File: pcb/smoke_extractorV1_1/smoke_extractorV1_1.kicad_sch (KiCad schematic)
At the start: 7 parts

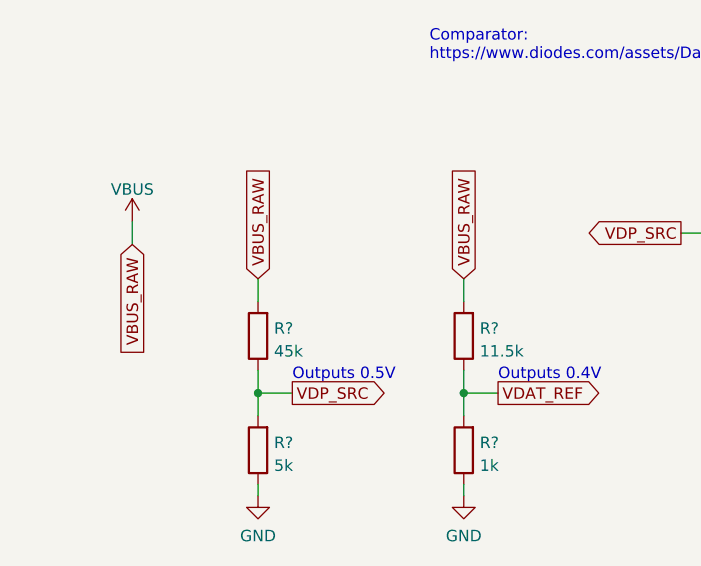
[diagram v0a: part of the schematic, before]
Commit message: Added the first comparator for the USB Data lines
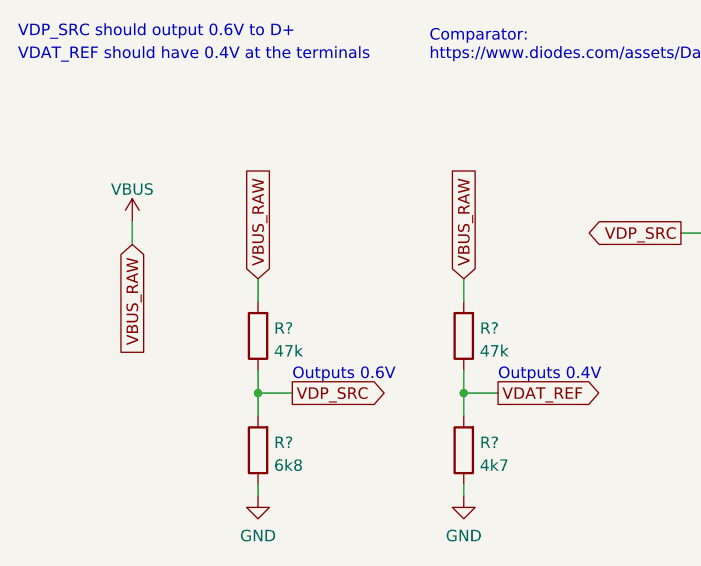
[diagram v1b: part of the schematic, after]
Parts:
- R?: value 1k -> 4k7
- R?: value 11.5k -> 47k
- R?: value 45k -> 47k
- R?: value 5k -> 6k8
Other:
- note added: "Outputs 0.6V"
- note added: "VDAT_REF should have 0.4V at the terminals"
- note added: "VDP_SRC should output 0.6V to D+"
- note removed: "Outputs 0.5V"
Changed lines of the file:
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@@
     (stroke (width 0) (type default) (color 0 0 0 0))
   )
+  (text "VDAT_REF should have 0.4V at the terminals\n" (at 12.7 6.35 0)
+    (effects (font (size 1.27 1.27)) (justify left bottom))
+  )
   (text "Outputs 0.4V" (at 66.04 41.91 0)
     (effects (font (size 1.27 1.27)) (justify left bottom))
   )
-  (text "Outputs 0.5V" (at 43.18 41.91 0)
+  (text "VDP_SRC should output 0.6V to D+" (at 12.7 3.81 0)
+    (effects (font (size 1.27 1.27)) (justify left bottom))
+  )
+  (text "Outputs 0.6V" (at 43.18 41.91 0)
     (effects (font (size 1.27 1.27)) (justify left bottom))
   )
@@
       (effects (font (size 1.27 1.27)) (justify right))
     )
-    (property "Value" "1k" (id 1) (at 64.008 51.2322 0)
+    (property "Value" "4k7" (id 1) (at 64.008 51.2322 0)
       (effects (font (size 1.27 1.27)) (justify right))
     )
@@
       (effects (font (size 1.27 1.27)) (justify right))
     )
-    (property "Value" "11.5k" (id 1) (at 64.008 38.5322 0)
+    (property "Value" "47k" (id 1) (at 64.008 38.5322 0)
       (effects (font (size 1.27 1.27)) (justify right))
     )
@@
       (effects (font (size 1.27 1.27)) (justify right))
     )
-    (property "Value" "45k" (id 1) (at 41.148 38.5322 0)
+    (property "Value" "47k" (id 1) (at 41.148 38.5322 0)
       (effects (font (size 1.27 1.27)) (justify right))
     )
@@
       (effects (font (size 1.27 1.27)) (justify right))
     )
-    (property "Value" "5k" (id 1) (at 41.148 51.2322 0)
+    (property "Value" "6k8" (id 1) (at 41.148 51.2322 0)
       (effects (font (size 1.27 1.27)) (justify right))
     )
@@
     )
     (path "/003a3556-27e1-4c94-8336-eff7b2d2f9bb"
-      (reference "R?") (unit 1) (value "1k") (footprint "")
+      (reference "R?") (unit 1) (value "4k7") (footprint "")
     )
     (path "/380a39d0-b84f-4b62-87a9-847ecd2b9168"
-      (reference "R?") (unit 1) (value "11.5k") (footprint "")
+      (reference "R?") (unit 1) (value "47k") (footprint "")
     )
     (path "/56ce3fcd-62bc-4dba-a6b1-ae8205ebf6db"
-      (reference "R?") (unit 1) (value "45k") (footprint "")
+      (reference "R?") (unit 1) (value "47k") (footprint "")
     )
     (path "/b683cc23-b225-4f7c-ab01-f58eb518a6d4"
@@
     )
     (path "/e38d534d-2172-4396-955c-5f0a970e41ae"
-      (reference "R?") (unit 1) (value "5k") (footprint "")
+      (reference "R?") (unit 1) (value "6k8") (footprint "")
     )
     (path "/e88e7d59-0051-411d-8d9c-5506936fb14d"

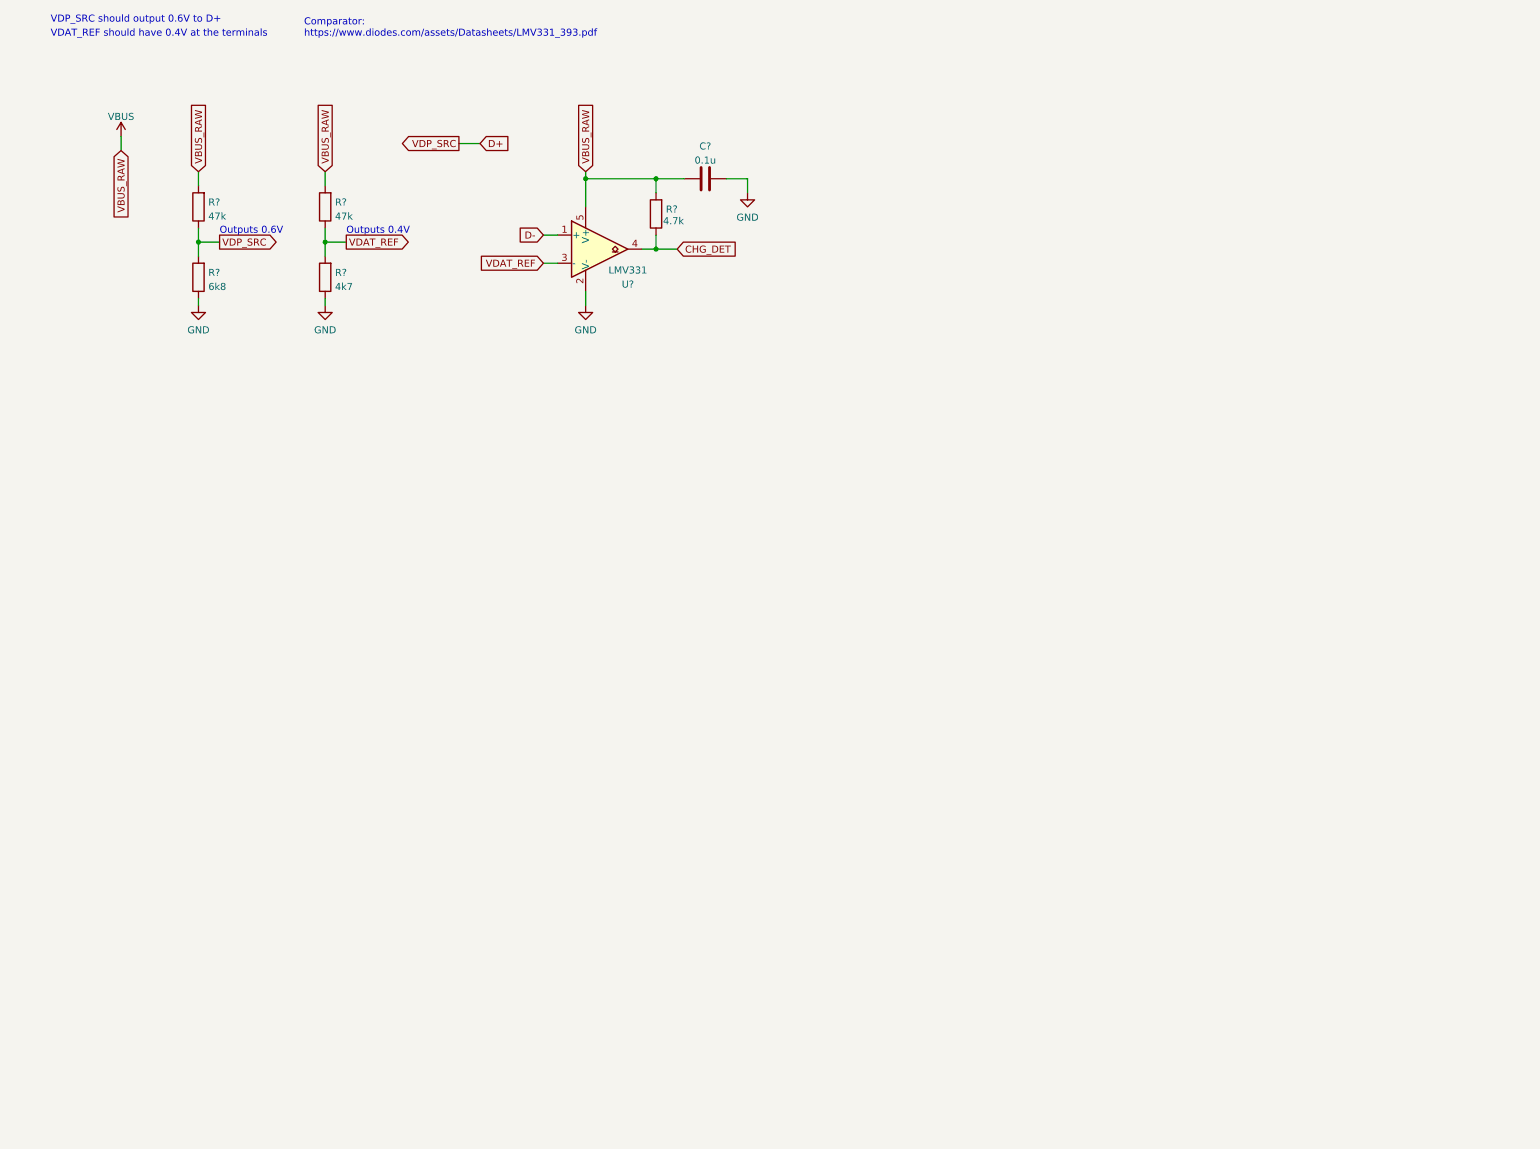
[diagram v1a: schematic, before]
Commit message: Added comparators circuit (D lines and CC lines) to the schematic
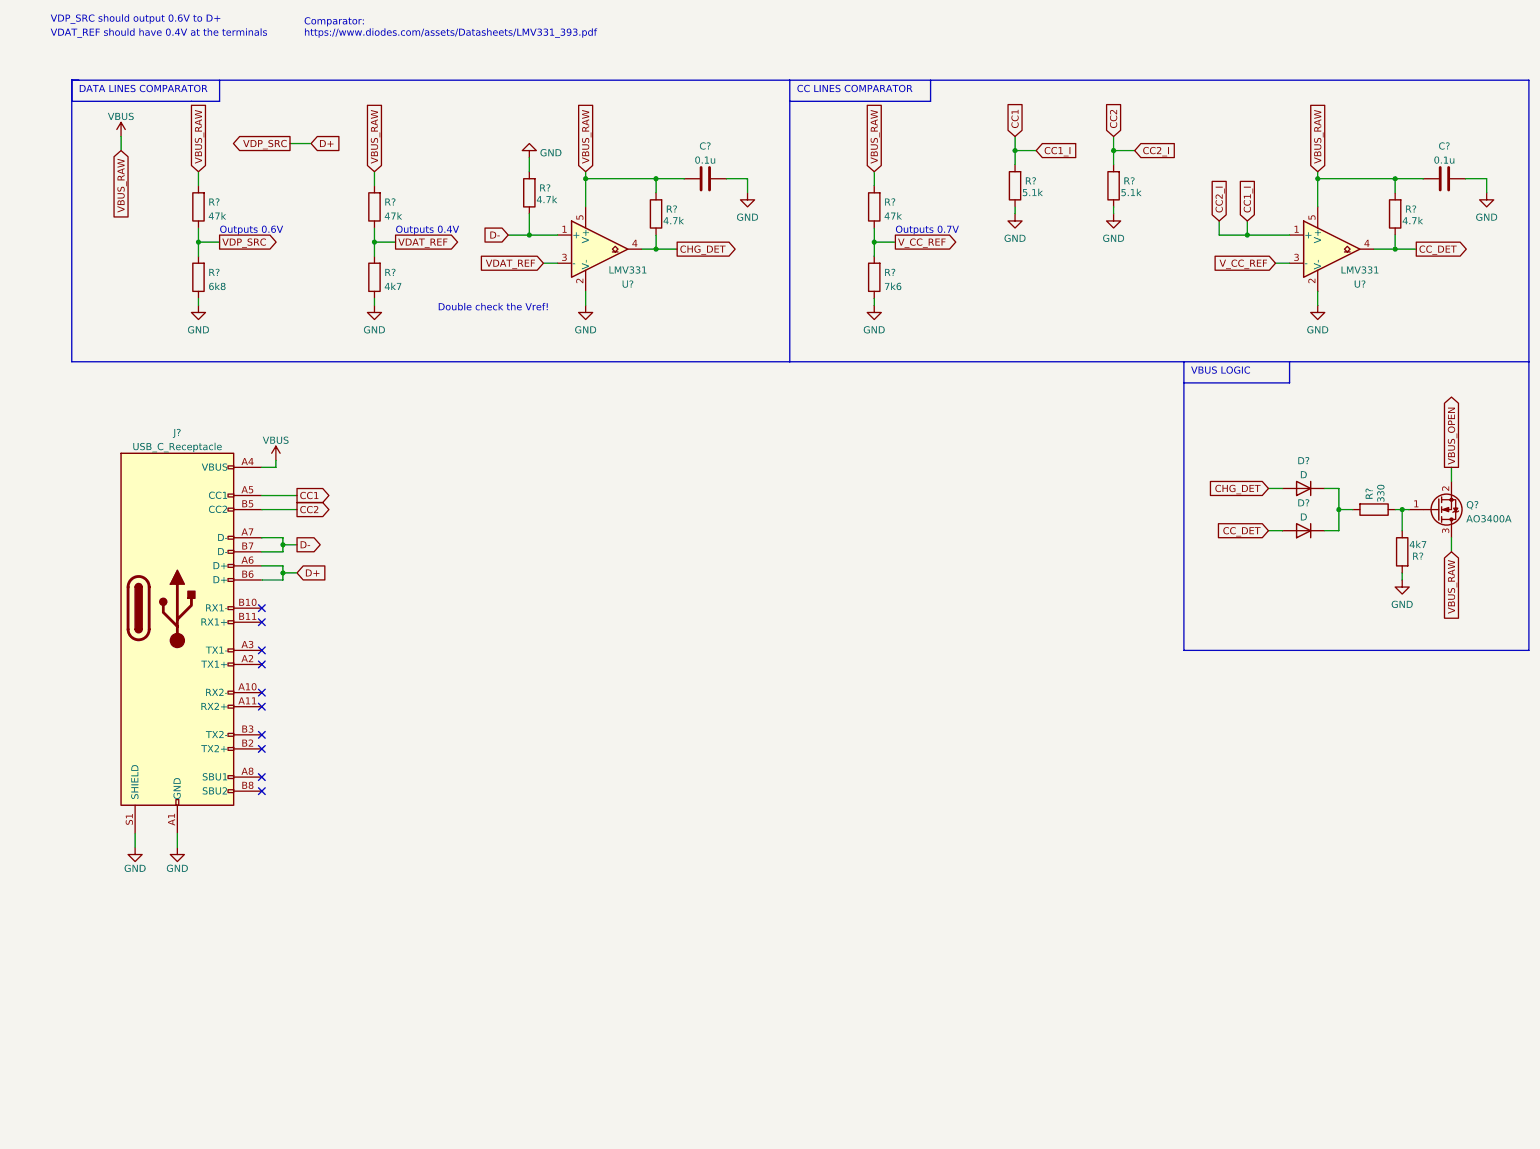
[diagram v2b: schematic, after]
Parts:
- added C?: 0.1u, symbol Device:C
- added D? (x2): D, symbol Device:D
- added J?: USB_C_Receptacle, symbol Connector:USB_C_Receptacle
- added Q?: AO3400A, Package_TO_SOT_SMD:SOT-23, symbol Transistor_FET:AO3400A
- added R?: 4k7, symbol Device:R
- added R? (x2): 5.1k, symbol Device:R
- added R?: 47k, symbol Device:R
- added R? (x2): 4.7k, symbol Device:R
- added R?: 330, symbol Device:R
- added R?: 7k6, symbol Device:R
- added U?: LMV331, symbol Comparator:LMV331
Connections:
- net CHG_DET: now also D?.2 (A)
- net D+: now also J?.A6 (D+), J?.B6 (D+)
- net D-: now also J?.A7 (D-), J?.B7 (D-), R?.1
- net GND: now also C?.2, J?.A1 (GND), J?.A12 (GND), J?.B1 (GND), J?.B12 (GND), J?.S1 (SHIELD), R?.1, R?.1, R?.1, R?.2, R?.2, U?.2 (V-)
- net VBUS: now also C?.1, J?.A4 (VBUS), J?.A9 (VBUS), J?.B4 (VBUS), J?.B9 (VBUS), Q?.3 (D), R?.2, R?.2, U?.5 (V+)
- new net: Q?.1 (G), R?.1, R?.1
- new net: D?.1 (K), D?.1 (K), R?.2
- new net CC1: J?.A5 (CC1), J?.B5 (CC2), R?.2, R?.2, U?.1 (+)
- new net CC_DET: D?.2 (A), R?.1, U?.4
- new net VBUS_OPEN: Q?.2 (S)
- new net V_CC_REF: R?.1, R?.2, U?.3 (-)
- no-connect marks 0 -> 10
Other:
- note added: "CC LINES COMPARATOR"
- note added: "DATA LINES COMPARATOR"
- note added: "Double check the Vref!"
- note added: "Outputs 0.7V"
- note added: "VBUS LOGIC"
- moved on the sheet: R?

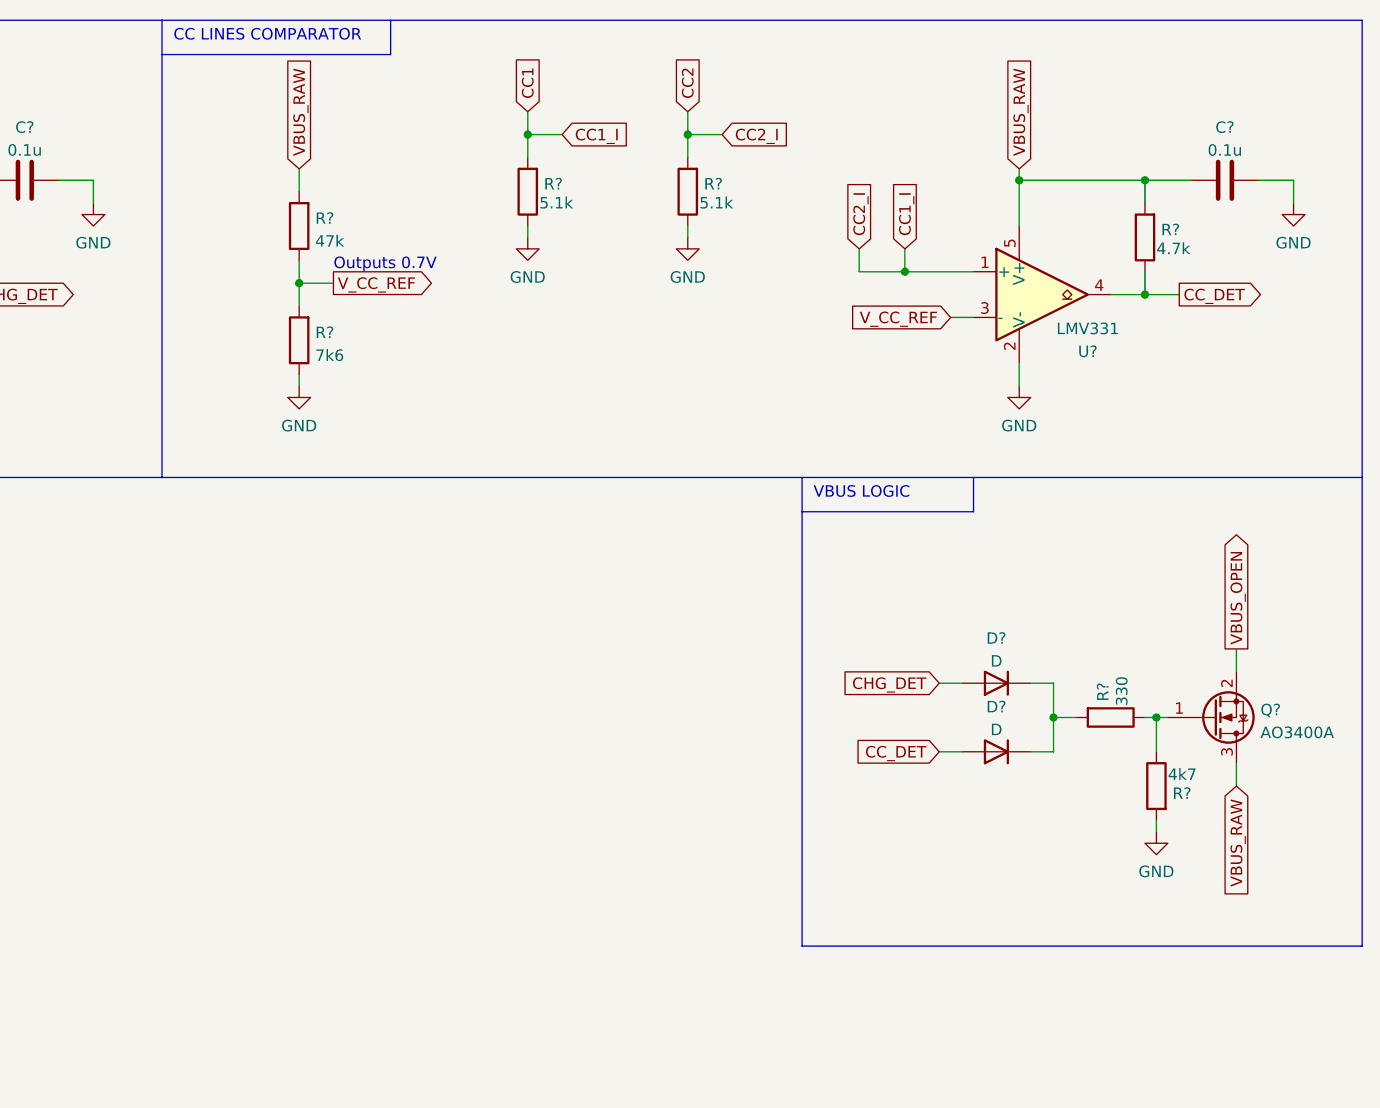
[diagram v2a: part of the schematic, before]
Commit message: Added missing comparator for the CC2 line.
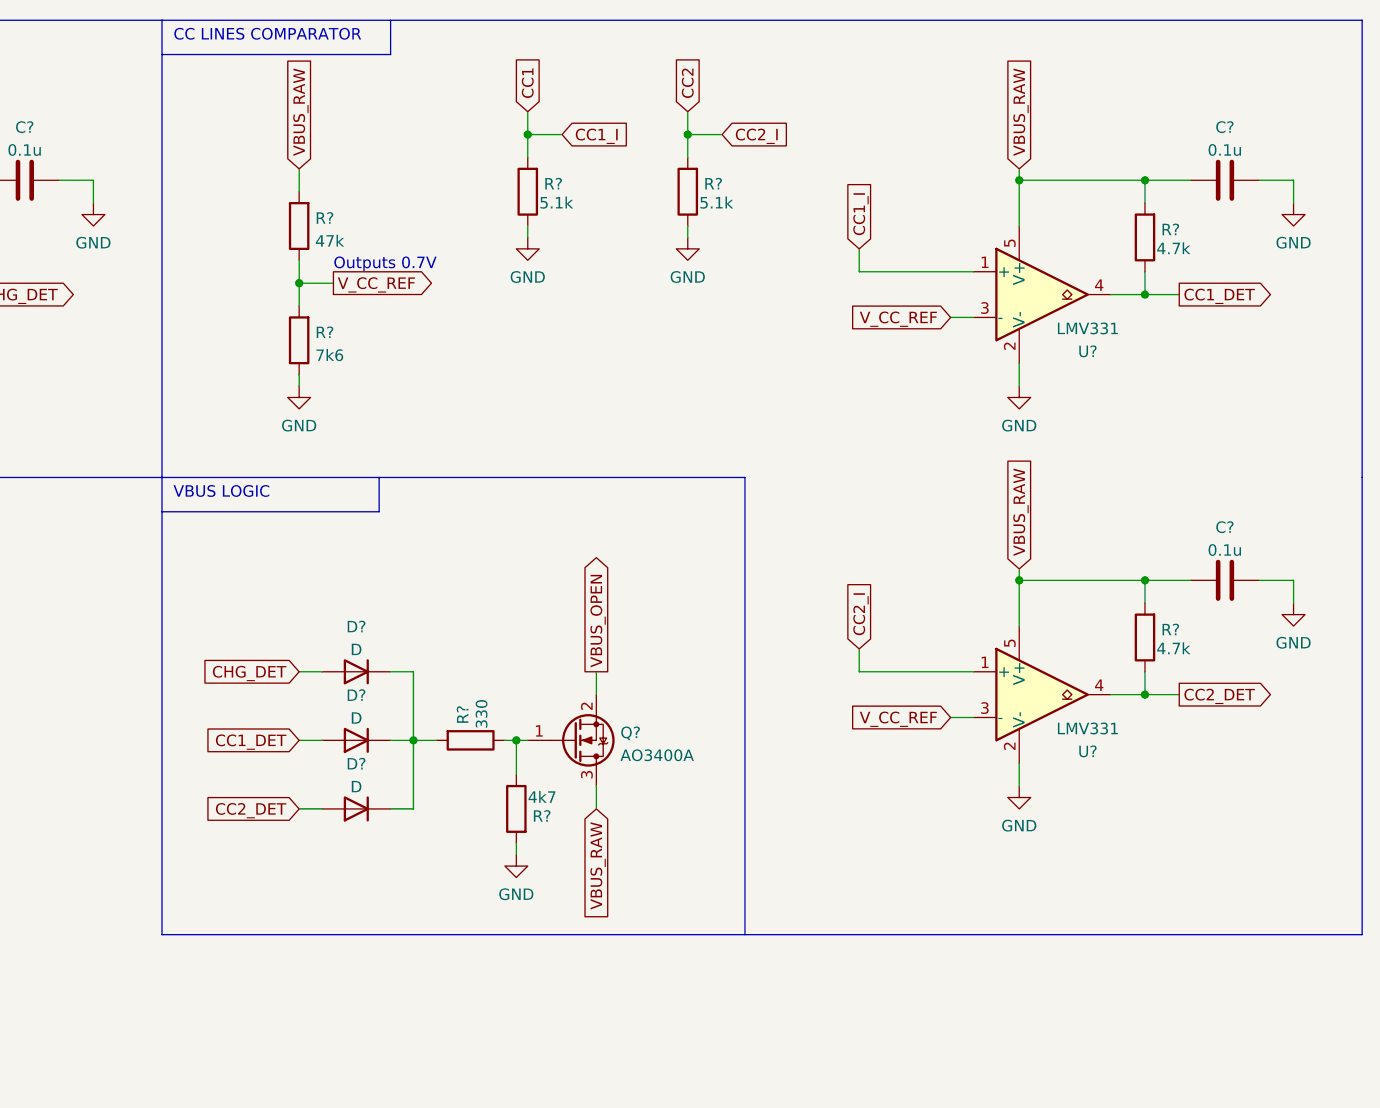
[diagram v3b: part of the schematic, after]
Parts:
- added C?: 0.1u, symbol Device:C
- added D?: D, symbol Device:D
- added R?: 4.7k, symbol Device:R
- added U?: LMV331, symbol Comparator:LMV331
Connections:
- net CC1: no longer J?.B5 (CC2), R?.2
- net GND: now also C?.2, U?.2 (V-)
- net VBUS: now also C?.1, R?.2, U?.5 (V+)
- net V_CC_REF: now also U?.3 (-)
- net at D?.1 (K), D?.1 (K), R?.2: now also D?.1 (K)
- net CC_DET renamed CC1_DET
- new net CC2: J?.B5 (CC2), R?.2, U?.1 (+)
- new net CC2_DET: D?.2 (A), R?.1, U?.4
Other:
- moved on the sheet: D?, Q?, R?

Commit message: Added a comment
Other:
- note added: "V- > V+ then Vout = 0V V- < V+ then Vout = 5V V- = Vref V+ = Vin"
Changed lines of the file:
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@@
+    (effects (font (size 1.27 1.27)) (justify left bottom))
+  )
+  (text "V- > V+ then Vout = 0V\nV- < V+ then Vout = 5V\n\nV- = Vref\nV+ = Vin"
+    (at 77.47 29.21 0)
     (effects (font (size 1.27 1.27)) (justify left bottom))
   )
